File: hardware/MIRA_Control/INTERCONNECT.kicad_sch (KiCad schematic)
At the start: 0 parts

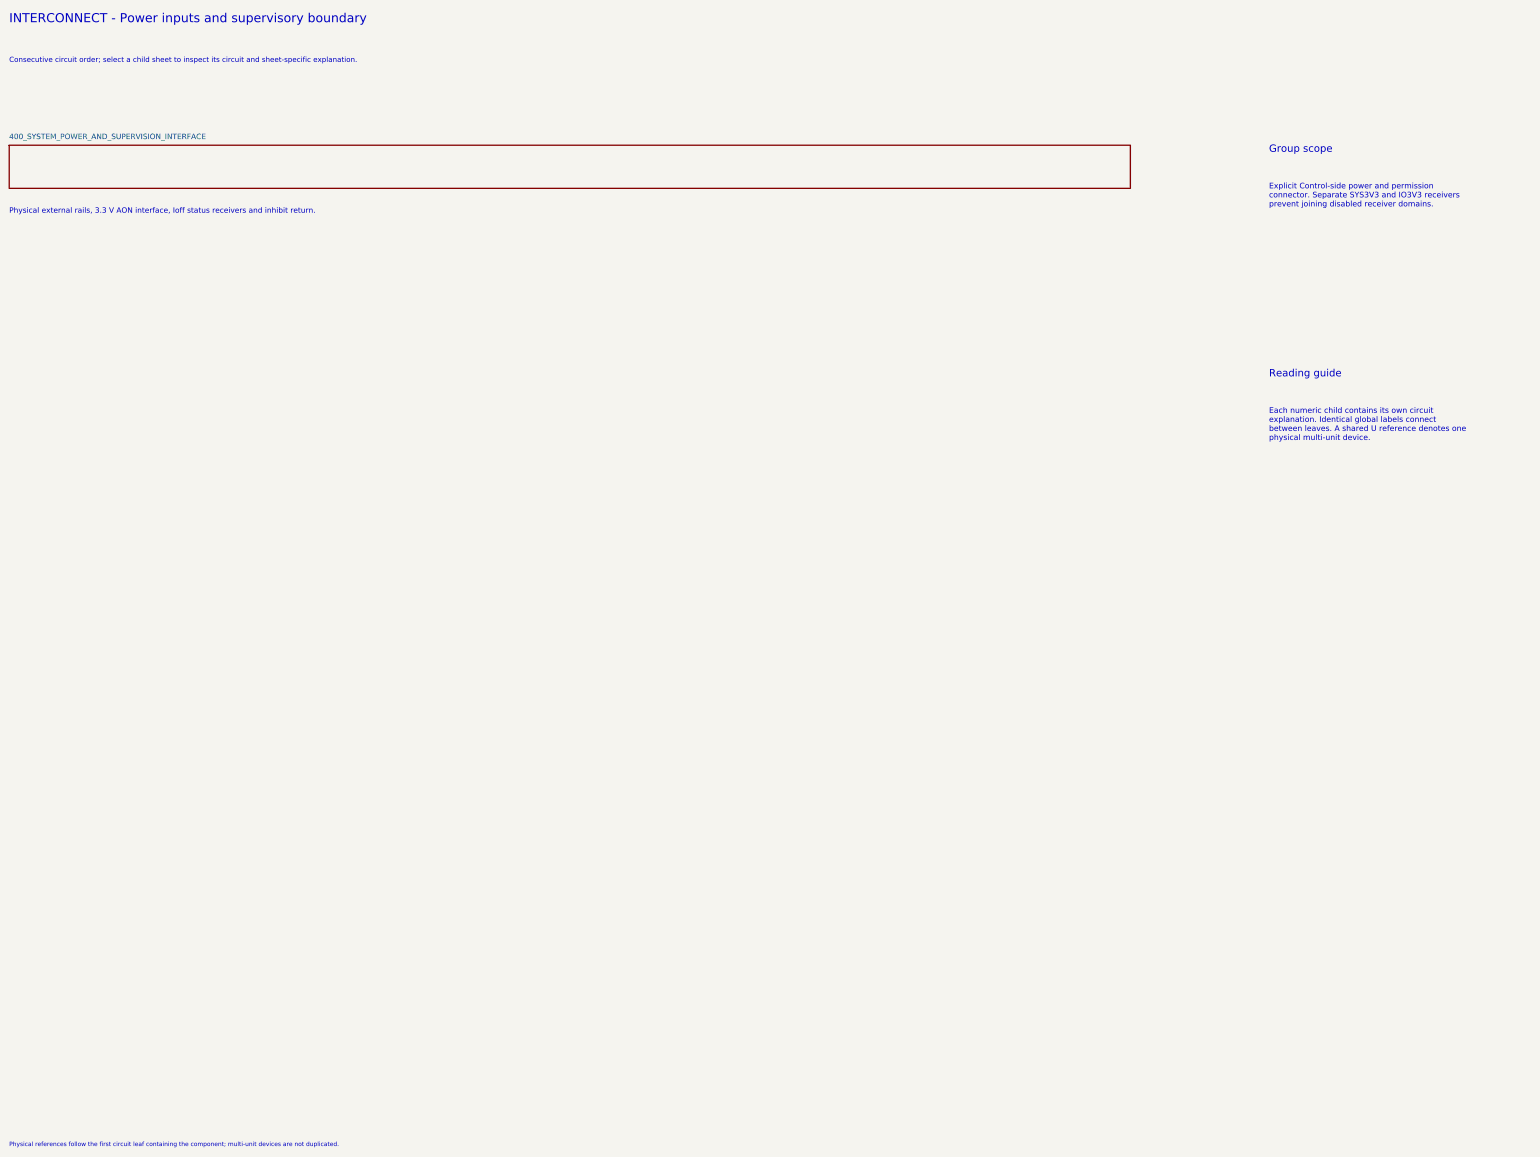
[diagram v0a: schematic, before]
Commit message: Distribute inter-board power across seven load zones and supervision
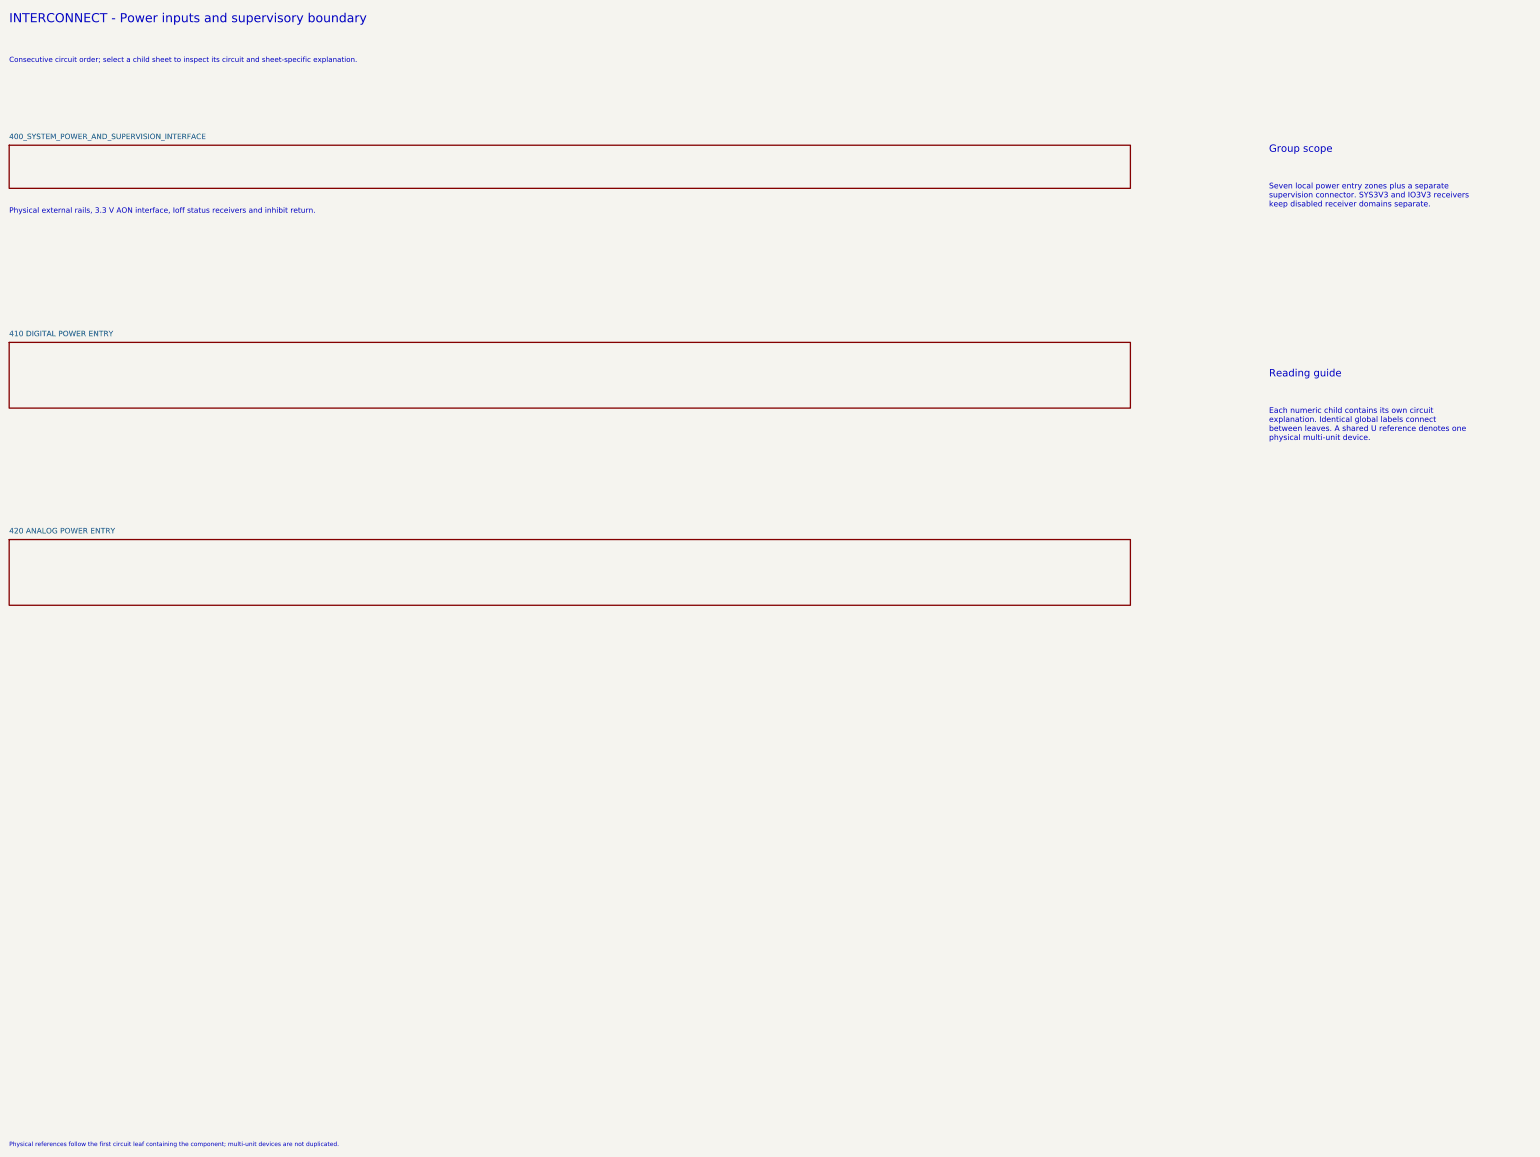
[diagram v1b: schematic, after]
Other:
- added sheet 410 DIGITAL POWER ENTRY (410_DISTRIBUTED_DIGITAL_POWER.kicad_sch)
- added sheet 420 ANALOG POWER ENTRY (420_DISTRIBUTED_ANALOG_POWER.kicad_sch)
- note added: "Seven local power entry zones plus a separate supervision connector. SYS3V3 and IO3V3 receivers keep disabled receiver domains separate."
- note removed: "Explicit Control-side power and permission connector. Separate SYS3V3 and IO3V3 receivers prevent joining disabled receiver domains."
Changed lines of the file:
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@@
 		)
 	)
-	(text "Explicit Control-side power and permission\nconnector. Separate SYS3V3 and IO3V3 receivers\nprevent joining disabled receiver domains."
+	(text "Seven local power entry zones plus a separate\nsupervision connector. SYS3V3 and IO3V3 receivers\nkeep disabled receiver domains separate."
 		(exclude_from_sim no)
 		(at 315 54.61 0)
@@
 		)
 	)
+(sheet (at 22.86 91.44) (size 260 15.24) (exclude_from_sim no) (in_bom yes) (on_board yes) (dnp no)
+ (stroke (width .254) (type solid)) (fill (color 0 0 0 0))
+ (property "Sheetname" "410 DIGITAL POWER ENTRY" (at 22.86 90.17 0) (effects (font (size 1.27 1.27)) (justify left bottom)))
+ (property "Sheetfile" "410_DISTRIBUTED_DIGITAL_POWER.kicad_sch" (at 22.86 107.95 0) (effects (font (size 1.016 1.016)) (justify left top) (hide yes)))
+ (instances (project "MIRA_Control" (path "/ad010b50-c509-466c-b833-d1667dfb0702/256d926f-b75a-42ae-a223-730b777ed784" (page "31")))))
+(sheet (at 22.86 137.16) (size 260 15.24) (exclude_from_sim no) (in_bom yes) (on_board yes) (dnp no)
+ (stroke (width .254) (type solid)) (fill (color 0 0 0 0))
+ (property "Sheetname" "420 ANALOG POWER ENTRY" (at 22.86 135.89 0) (effects (font (size 1.27 1.27)) (justify left bottom)))
+ (property "Sheetfile" "420_DISTRIBUTED_ANALOG_POWER.kicad_sch" (at 22.86 153.67 0) (effects (font (size 1.016 1.016)) (justify left top) (hide yes)))
+ (instances (project "MIRA_Control" (path "/ad010b50-c509-466c-b833-d1667dfb0702/256d926f-b75a-42ae-a223-730b777ed784" (page "32")))))
 )
